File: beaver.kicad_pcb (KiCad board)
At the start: 8 copper layers, 31.5 x 44.5 mm, 59 parts, among them J1 Conn_01x17, J2 Conn_01x17, J3 NFC, J4 USB_C_Receptacle_USB2.0, J5 Conn_01x04_Male, SW1 RESET, SW2 USER P0.17, U1 AZ1117-3.3, U2 nRF52840, U3 USBLC6-2SC6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

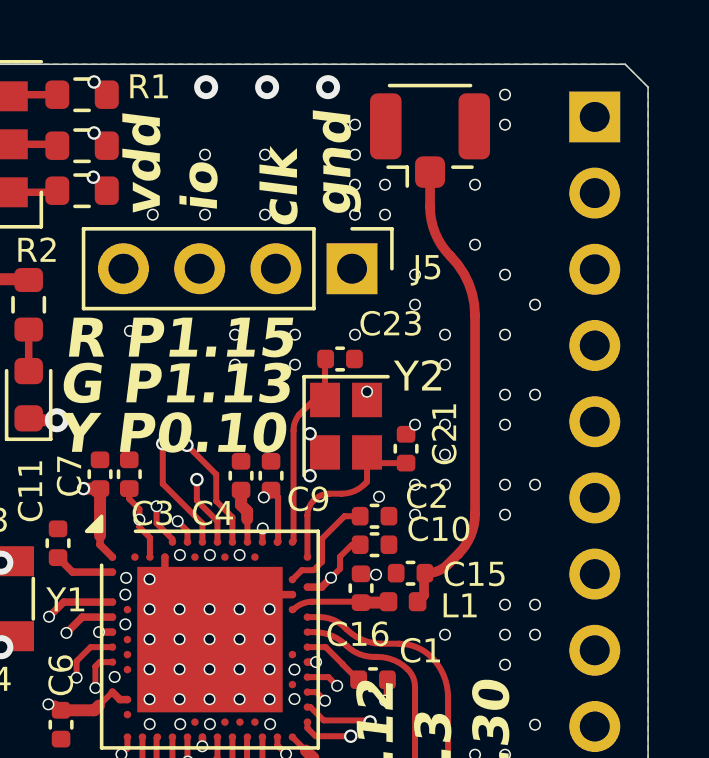
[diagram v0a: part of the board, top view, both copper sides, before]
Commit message: switch stackup for cost measures
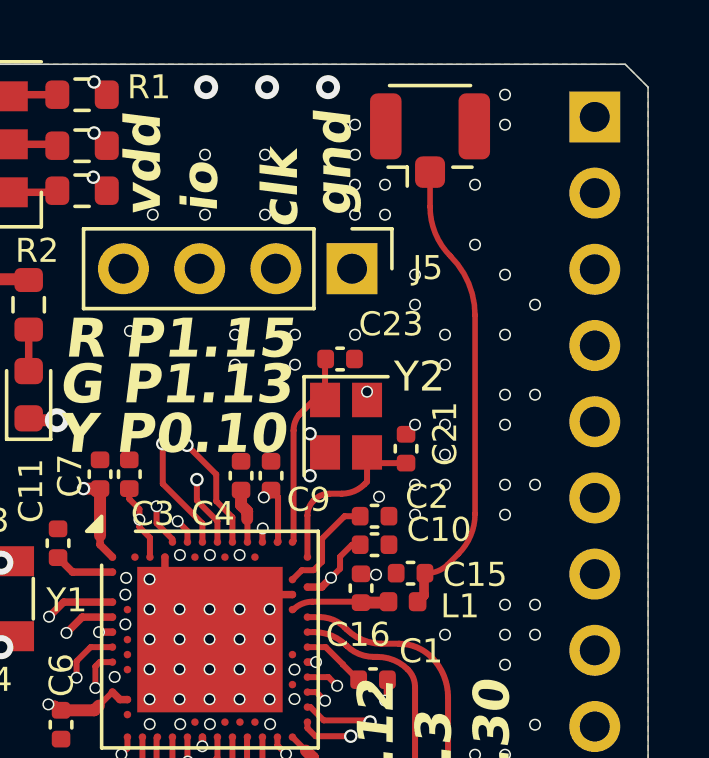
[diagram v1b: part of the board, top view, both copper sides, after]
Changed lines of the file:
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@@
 		(start 170.344 79.069166)
 		(end 170.344 77.916)
-		(width 0.324358)
+		(width 0.185674)
 		(layer "F.Cu")
 		(net 1)
@@
 		(start 170.936845 90.993155)
 		(end 171.292848 90.63717)
-		(width 0.324358)
+		(width 0.185674)
 		(layer "F.Cu")
 		(net 1)
@@
 		(start 170.174 91.286)
 		(end 170.229786 91.286)
-		(width 0.324358)
+		(width 0.185674)
 		(layer "F.Cu")
 		(net 1)
@@
 		(start 171.844 89.306618)
 		(end 171.844 82.690497)
-		(width 0.324358)
+		(width 0.185674)
 		(layer "F.Cu")
 		(net 1)
@@
 		(mid 170.521676 79.962404)
 		(end 170.344 79.069166)
-		(width 0.324358)
+		(width 0.185674)
 		(layer "F.Cu")
 		(net 1)
@@
 		(mid 170.612469 91.209895)
 		(end 170.936845 90.993155)
-		(width 0.324358)
+		(width 0.185674)
 		(layer "F.Cu")
 		(net 1)
@@
 		(mid 171.70076 90.026711)
 		(end 171.844 89.306618)
-		(width 0.324358)
+		(width 0.185674)
 		(layer "F.Cu")
 		(net 1)
@@
 		(mid 171.631837 81.623881)
 		(end 171.027655 80.719655)
-		(width 0.324358)
+		(width 0.185674)
 		(layer "F.Cu")
 		(net 1)

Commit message: switch to 6 layer stackup
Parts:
- D2: value Y P0.10 -> Y P1.13
- D3: value G P1.13 -> G P1.15
- D4: value R P1.15 -> R P0.2
- D5: value USB IN -> PWR
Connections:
- C22 pad 1: /RESET -> /USER_BUT
- C24 pad 1: /USER_BUT -> /RESET
- D2 pad 1: /P1.10 -> /P1.13
- D3 pad 1: /P1.13 -> /P1.15
- D4 pad 1: /P1.15 -> /P0.2
- J1 pad 4: /P0.31 -> /P0.29
- J1 pad 5: /P0.5 -> /P0.31
- J1 pad 6: /P0.2 -> /P0.5
- J2 pad 1: /P0.29 -> /P1.10
- R1 pad 2: /P1.12 -> /P0.30
- R5 pad 2: /P0.3 -> /P1.12
- R6 pad 2: /P0.30 -> /P0.3
- R7 pad 2: /RESET -> /USER_BUT
- R8 pad 2: /USER_BUT -> /RESET
- SW1 pad 1: /RESET -> /USER_BUT
- SW2 pad 1: /USER_BUT -> /RESET
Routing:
- net /P1.10: track 9.78 -> 20.4 mm, vias 2 -> 1
- net /P0.29: track 27.3 -> 19.0 mm
- net /P1.15: track 18.2 -> 11.4 mm
- net /P0.2: track 18.1 -> 13.7 mm, vias 1 -> 2
- net /RESET: track 29.5 -> 25.3 mm
- net /P0.3: track 21.5 -> 17.5 mm
- net /P1.12: track 23.0 -> 19.1 mm
- net /P1.13: track 13.2 -> 9.75 mm
- net /USER_BUT: track 24.6 -> 27.5 mm
- net /P0.31: track 17.0 -> 15.5 mm
- net /P0.25: track 16.1 -> 14.7 mm
- net /P0.20: track 17.3 -> 16.4 mm
- net /P0.30: track 20.6 -> 21.5 mm
- net /P0.12: track 18.2 -> 17.4 mm
- net /P0.13: track 19.5 -> 18.7 mm
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- removed copper zone on In6.Cu, net GNDREF
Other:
- copper layers 8 -> 6
- board text added: "1.10"
- board text added: "R P0.30 G P1.12 B P0.3"
- board text added: "RST"
- board text removed: "0.2"
- board text removed: "R P1.12 G P0.3 B P0.30"
